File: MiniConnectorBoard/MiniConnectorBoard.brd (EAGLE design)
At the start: 31.1 x 68.6 mm, 4 parts

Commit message: MiniConnectorBoard - first cut
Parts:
- added JP3: NONE, MiniConnectorBoard:1X20
- JP2: device HeaderConnectorBoard:2X20 -> MiniConnectorBoard:1X20
- moved R1 10.6 mm to (9.53, 3.17), turned to 270 degrees
- moved JP2 8.35 mm to (12.1, 32.4)
- moved JP1 3.72 mm to (15.2, 32.4)
- moved LED1 1.42 mm to (4.45, 3.17)
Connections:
- net 10/MOSI: now also JP3.10; no longer JP2.20
- net 11/CLK: now also JP3.12; no longer JP2.24
- net 12: now also JP2.16; no longer JP2.31
- net 13: now also JP3.17; no longer JP2.34
- net 14/TX: now also JP2.4; no longer JP2.7
- net 15/RX: now also JP2.5; no longer JP2.9
- net 16: now also JP2.18; no longer JP2.35
- net 17/RTS: now also JP3.6; no longer JP2.12
- net 18: now also JP2.6; no longer JP2.11
- net 19: now also JP3.18; no longer JP2.36
- net 2/SDA: now also JP3.2; no longer JP2.4
- net 20: now also JP2.19; no longer JP2.37
- net 21: now also JP2.20; no longer JP2.39
- net 22: now also JP3.8; no longer JP2.16
- net 23: now also JP2.8; no longer JP2.15
- net 24: now also JP2.9; no longer JP2.17
- net 25: now also JP2.11; no longer JP2.21
- net 26: now also JP3.19; no longer JP2.38
- net 27: now also JP3.7; no longer JP2.14
- net 3.3V_1: now also JP3.1; no longer JP2.2
- net 3.3V_2: now also JP3.9; no longer JP2.18
- net 3/SCL: now also JP3.3; no longer JP2.6
- net 4: now also JP3.4; no longer JP2.8
- net 5: now also JP3.15; no longer JP2.30
- net 5V_1: now also JP2.2; no longer JP2.3
- net 6: now also JP3.16; no longer JP2.32
- net 7/CE1: now also JP2.13; no longer JP2.25
- net 8/CE0: now also JP2.12; no longer JP2.23
- net 9/MISO: now also JP3.11; no longer JP2.22
- net GND: now also JP3.5; no longer JP2.10
- net GND2: now also JP3.13; no longer JP2.26
- net GND3: now also JP2.10; no longer JP2.19
- net GND4: now also JP2.7; no longer JP2.13
- net GND5: now also JP2.3; no longer JP2.5
- net GND6: now also JP3.20; no longer JP2.40, R1.1
- net GND7: now also JP2.17, R1.1; no longer JP2.33
- net GND8: now also JP2.15; no longer JP2.29
- net ID1: now also JP3.14; no longer JP2.28
- net ID2: now also JP2.14; no longer JP2.27
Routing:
- net GND6: track 19.5 -> 3.26 mm
- net N$1: track 19.7 -> 5.17 mm
- net 5: track 16.0 -> 3.17 mm
- net 14/TX: track 16.0 -> 3.18 mm
- net 4: track 16.0 -> 3.17 mm
- net GND8: track 16.0 -> 3.18 mm
- net GND: track 16.0 -> 3.18 mm
- net ID1: track 16.0 -> 3.18 mm
- net 6: track 16.0 -> 3.18 mm
- net 3/SCL: track 16.0 -> 3.18 mm
- net 17/RTS: track 16.0 -> 3.19 mm
- net GND2: track 16.0 -> 3.19 mm
- net 13: track 16.0 -> 3.19 mm
- net 2/SDA: track 16.0 -> 3.19 mm
- net 7/CE1: track 16.0 -> 3.24 mm
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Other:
- board size 31.1 x 68.6 mm -> 30.5 x 65 mm
- board text added: "Rev-01a (c) 2016 Ready Set STEM"
- board text removed: "Rev-02a (c) 2016 Ready Set STEM"

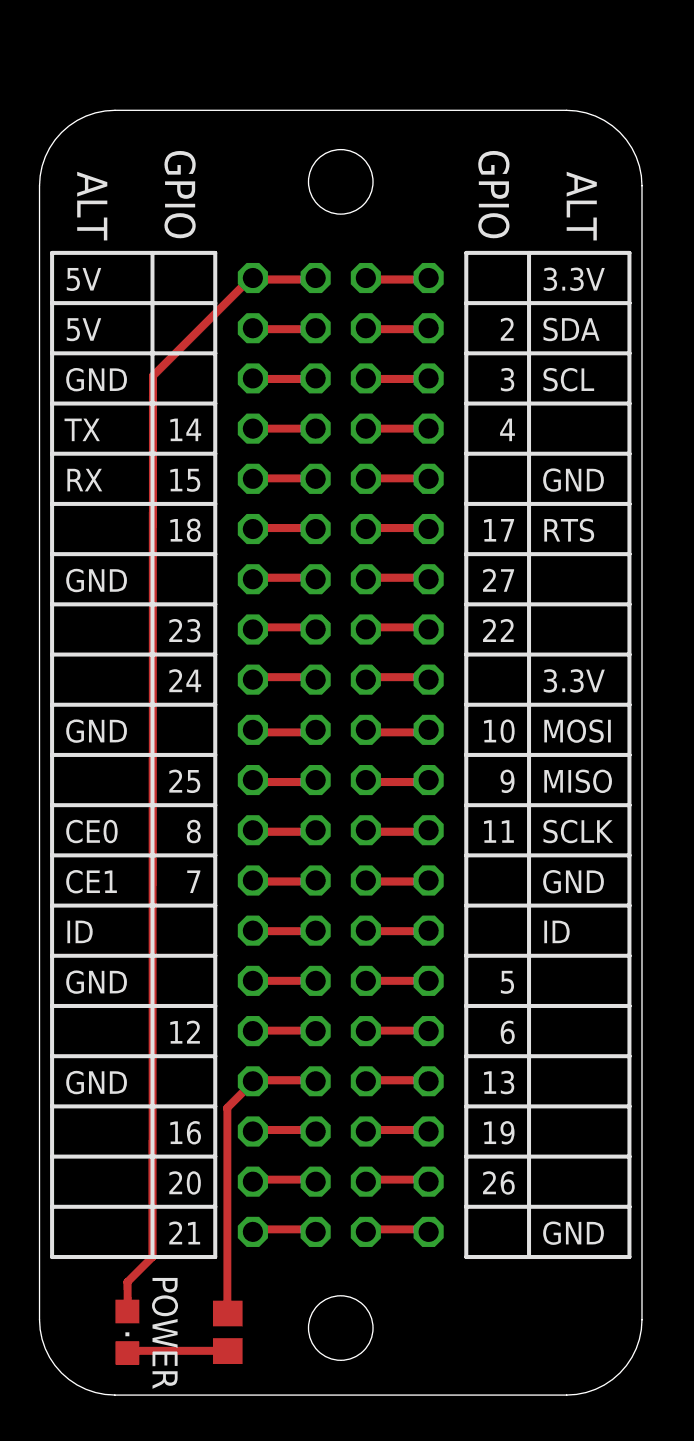
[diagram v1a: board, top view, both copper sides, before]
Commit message: MiniConnectorBoard - removed power, added logo, Rev-01b
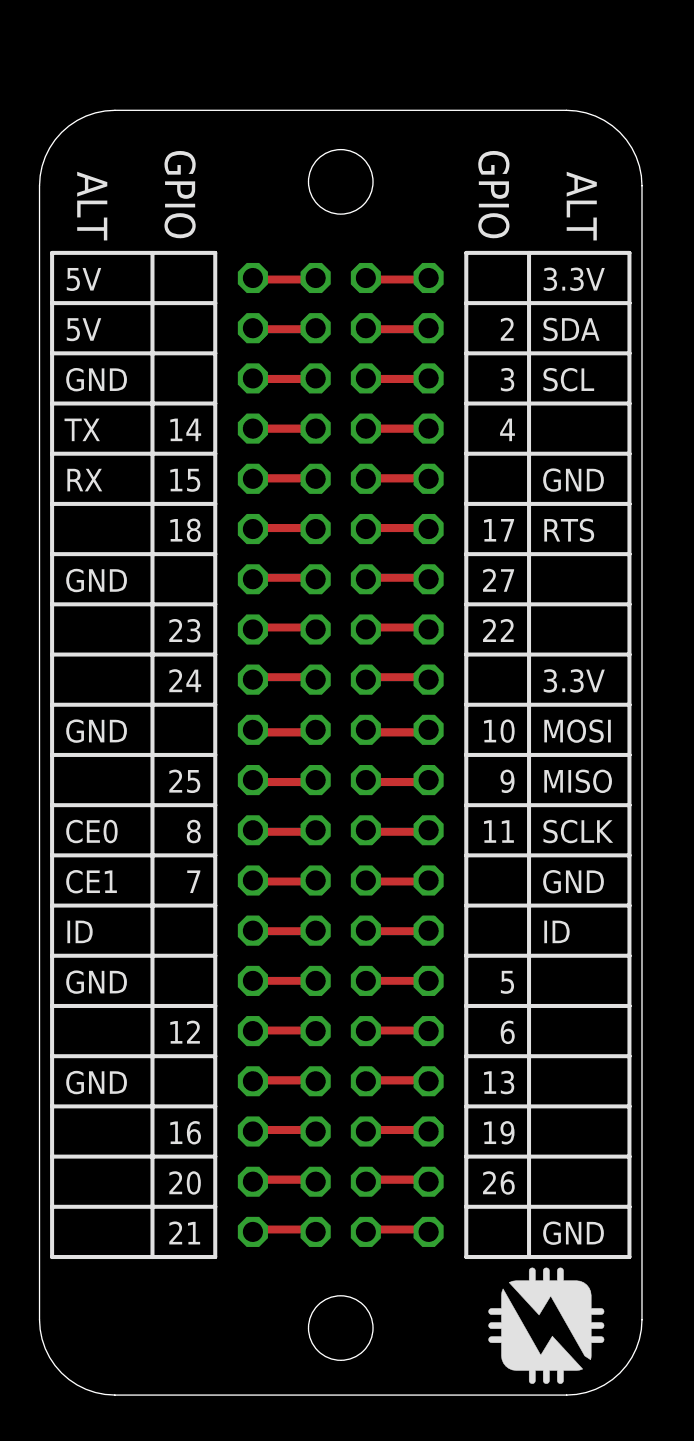
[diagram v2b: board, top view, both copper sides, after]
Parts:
- removed LED1: 475-1410-2-ND, led:CHIPLED_0805
- removed R1: 200, resistor:R0805
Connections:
- removed net N$1: LED1.C, R1.2
- net 5V_2: no longer LED1.A
- net GND7: no longer R1.1
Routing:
- net 5V_2: track 58.2 -> 3.28 mm
- net GND7: track 15.5 -> 3.24 mm
- net N$1: track 5.17 -> 0.00 mm
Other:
- board text added: "Rev-01b (c) 2016 Ready Set STEM"
- board text removed: "POWER"
- board text removed: "Rev-01a (c) 2016 Ready Set STEM"
